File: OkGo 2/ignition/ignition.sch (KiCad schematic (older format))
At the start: 44 parts, among them K101 16A SPST, P101 BATT, P102 BATT, P103 CHARGE_CASE, P104 CHARGE_CASE, P105 CHARGE_JST_XH, P106 SMA, SW101 LATCHING PUSH, U101 SWD, U102 BEZEL, U103 RFM95W, U104 STM32F071CBT6, U105 TSR 0.5-2433, Y101 8MHz

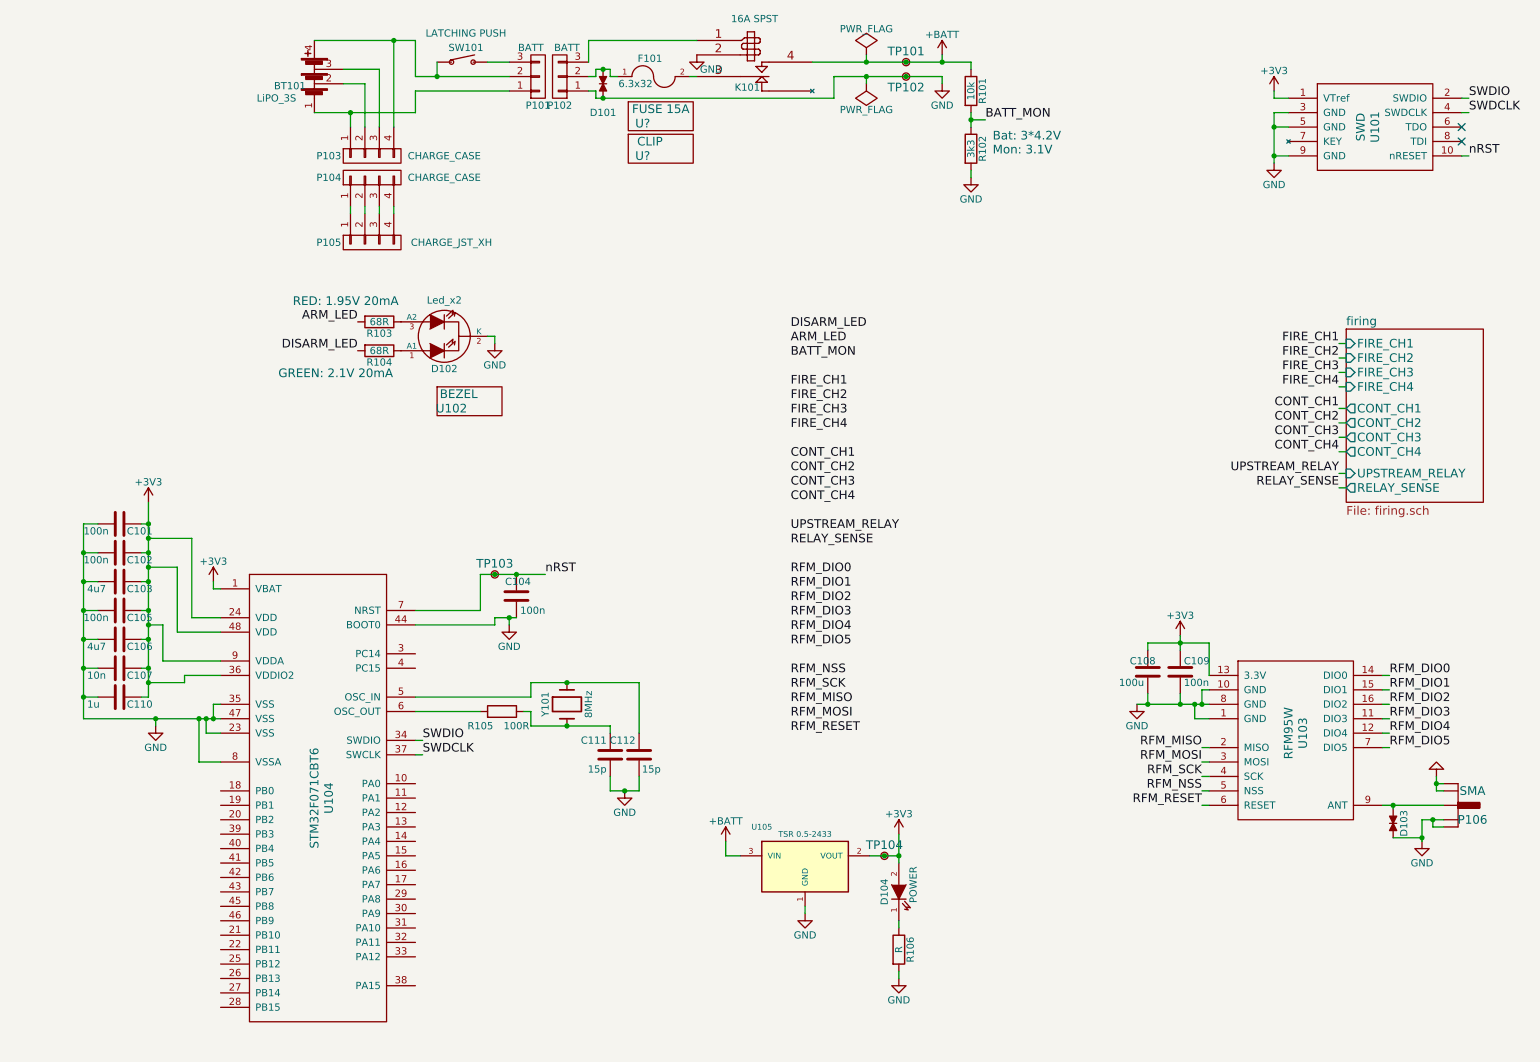
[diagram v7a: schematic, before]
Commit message: Footprinting on ignition + TPs
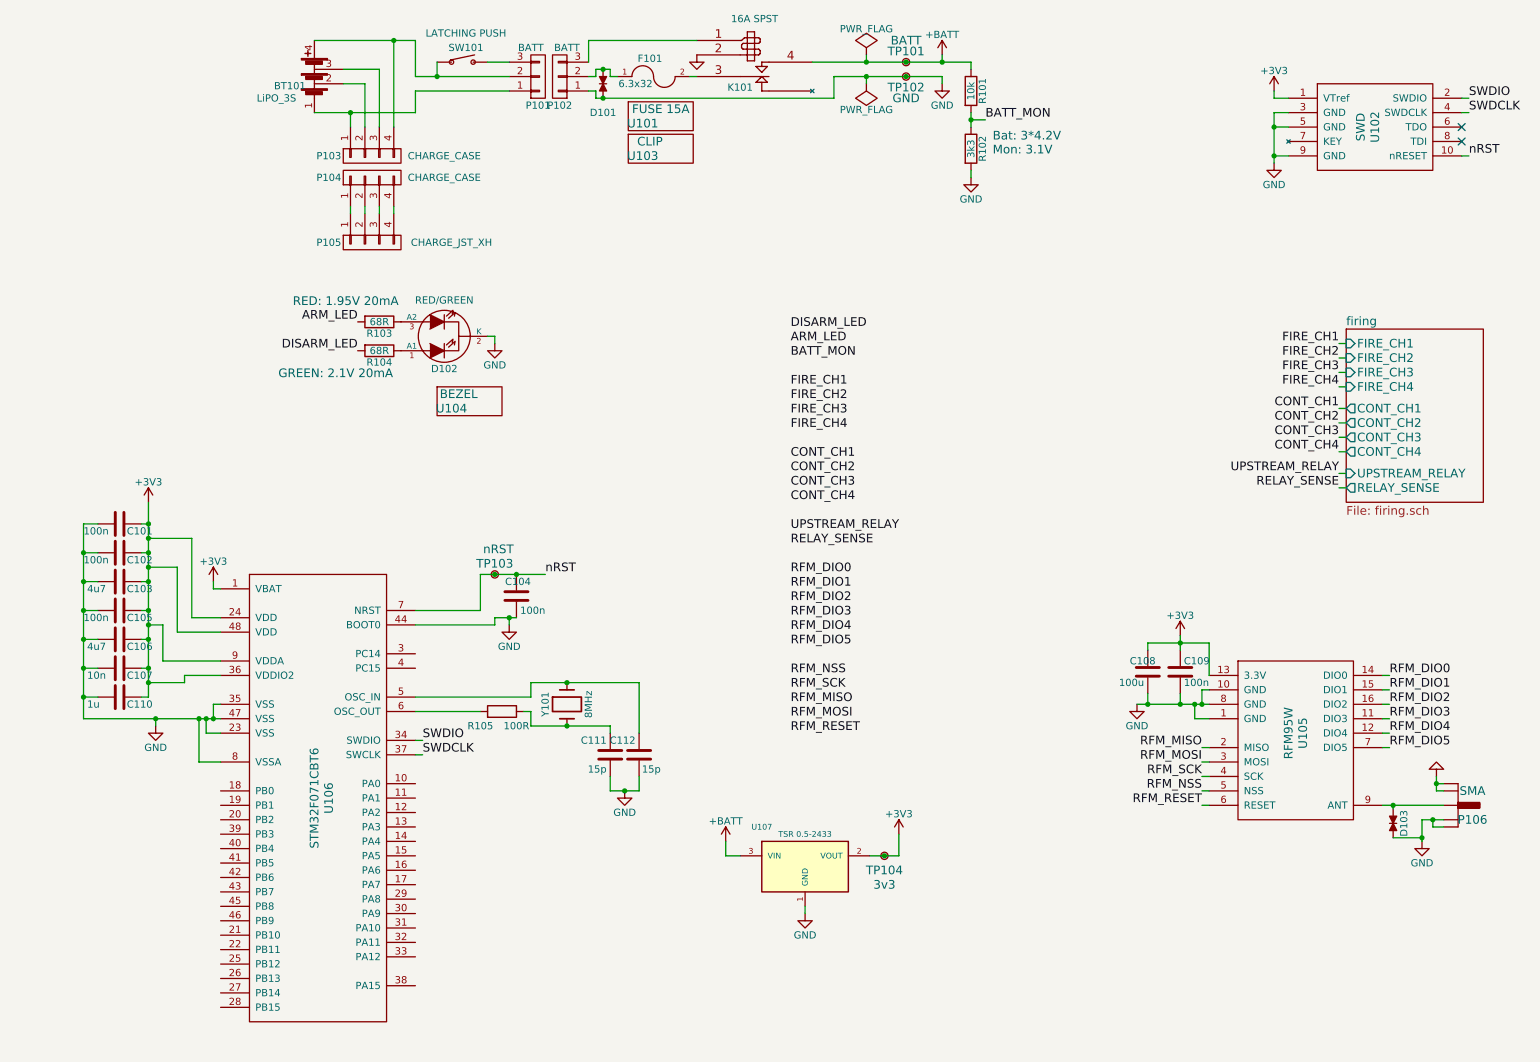
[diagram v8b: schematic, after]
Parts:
- removed D104: POWER, symbol LED
- removed R106: R, Resistors_SMD:R_0805_HandSoldering, symbol R
- D102: value Led_x2 -> RED/GREEN
- TP101: value TestPoint -> BATT; footprint (none) -> common:TESTPOINT
- TP102: value TestPoint -> GND; footprint (none) -> common:TESTPOINT
- TP103: value TestPoint -> nRST; footprint (none) -> common:TESTPOINT
- TP104: value TestPoint -> 3v3; footprint (none) -> common:TESTPOINT
- U105: renamed from U103; footprint (none) -> common:RFM95W
- gave numbers to parts that had none: 2
- renumbered U101 to U102, U102 to U104, U104 to U106, U105 to U107
